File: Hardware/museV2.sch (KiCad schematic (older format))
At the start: 164 parts, among them J1 ATX24, J2 ATX24, P1 RCA_Stero_Jack, P10 AI_RGB, P11 CONN_01X04, P12 AI_RGB, P13 AI_RGB, P14 AI_RGB, P15 AI_RGB, P16 CONN_01X04, P17 AI_RGB, P18 AI_RGB, P19 AI_RGB, P2 CONN_01X06, P20 AI_RGB, P21 AI_RGB, P22 CONN_01X04, P23 AI_RGB, P24 AI_RGB, P25 AI_RGB, P3 3.5mm_Audio, P4 RCA_Stero_Jack, P5 3.5mm_Audio, P6 CONN_01X04, P7 AI_RGB, P8 AI_RGB, P9 AI_RGB, Q1 MOSFET_N, Q10 MOSFET_N, Q11 MOSFET_N, Q12 MOSFET_N, Q13 MOSFET_N, Q2 MOSFET_N, Q3 MOSFET_N, Q4 MOSFET_N, Q5 MOSFET_N, Q6 MOSFET_N, Q7 BSS138, Q8 MOSFET_N, Q9 MOSFET_N, SW1 PWR_BTN, U1 POM-3535L-3-R, U10 PCM1863, U11 PCM1796, U2 PLR135/T10, U3 POM-3535L-3-R, U4 PLT133/T10W, U5 POM-3535L-3-R, U6 POM-3535L-3-R, U7 PCM9211, U8 EdisonConnector, U9 LP38692, X1 24.576 MHz

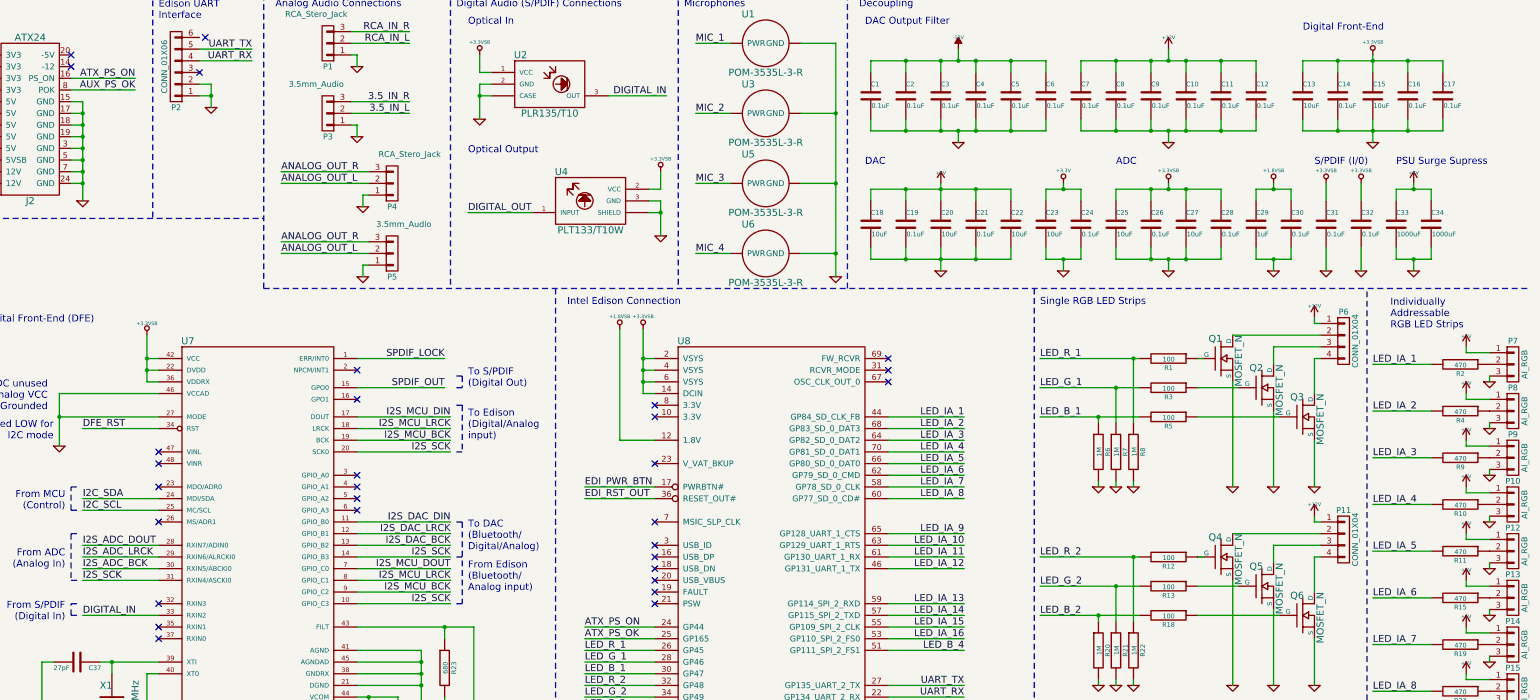
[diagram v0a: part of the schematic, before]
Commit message: Fixed SPDIF labels,
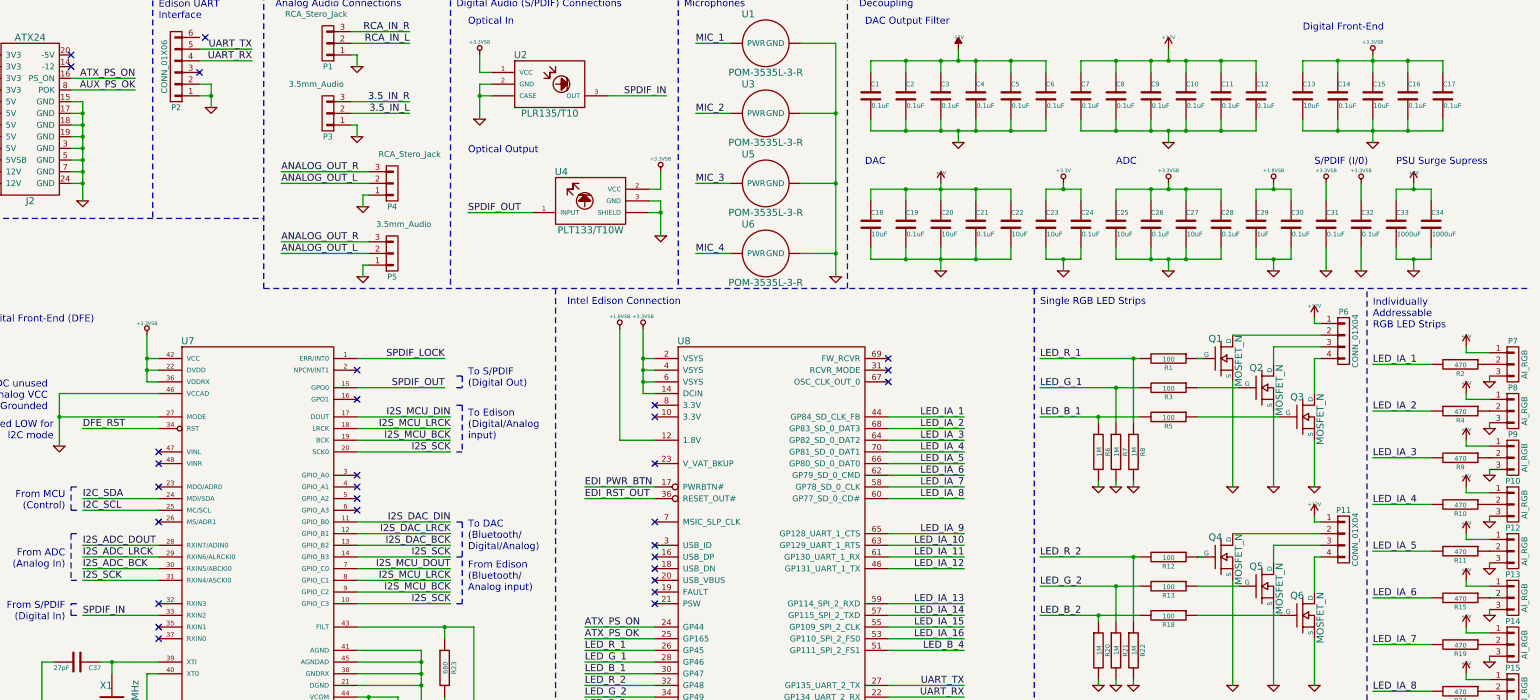
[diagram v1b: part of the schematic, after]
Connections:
- net Audio_Filter/ANALOG_OUT+ is gone; now on net Audio_Filter/ANALOG_OUT+: U11.25 (IOUT_L+)
- net Audio_Filter/ANALOG_OUT- is gone; now on net Audio_Filter/ANALOG_OUT-: U11.26 (IOUT_L-)
- net DIGITAL_OUT is gone; now on net SPDIF_OUT: U4.1 (INPUT)
- net Audio_Filter/ANALOG_OUT+: no longer U11.17 (IOUT_R+)
- net Audio_Filter/ANALOG_OUT-: no longer U11.18 (IOUT_R-)
- net DIGITAL_IN renamed SPDIF_IN
- new net Audio_Filter/ANALOG_OUT+: U11.17 (IOUT_R+)
- new net Audio_Filter/ANALOG_OUT-: U11.18 (IOUT_R-)
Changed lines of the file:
@@
 $EndComp
 Text Label 6950 2400 0    60   ~ 0
-DIGITAL_OUT
+SPDIF_OUT
 Text Label 8650 1400 2    60   ~ 0
-DIGITAL_IN
+SPDIF_IN
 $Comp
 L GND-RESCUE-museV2 #PWR07
@@
 NoConn ~ 4300 6050
 Text Label 3650 5850 0    60   ~ 0
-DIGITAL_IN
+SPDIF_IN
 Text Notes 12500 2000 0    60   ~ 0
 ADC
@@
 Text Notes 11850 3200 0    60   ~ 0
 Single RGB LED Strips
-Text Notes 14850 3400 0    60   ~ 0
+Text Notes 14700 3400 0    60   ~ 0
 Individually \nAddressable\nRGB LED Strips
 $Comp

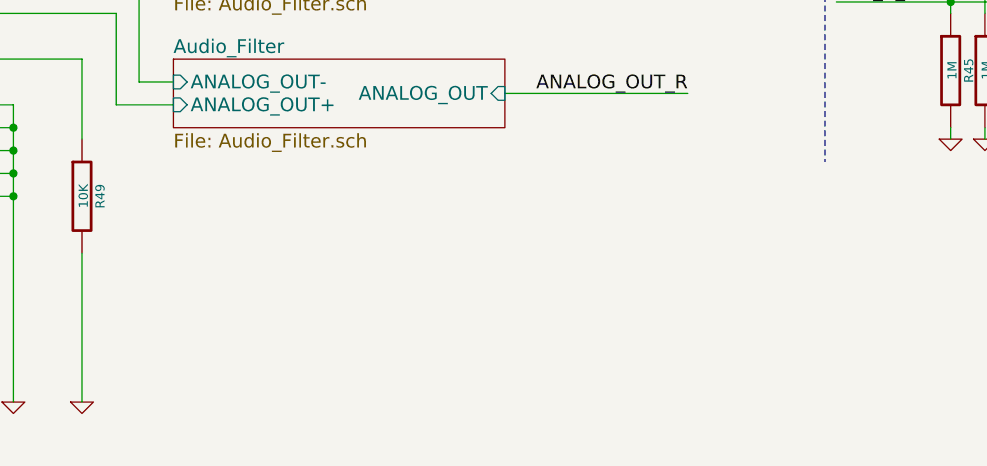
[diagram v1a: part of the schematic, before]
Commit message: Added split rail PS for DAC SB power
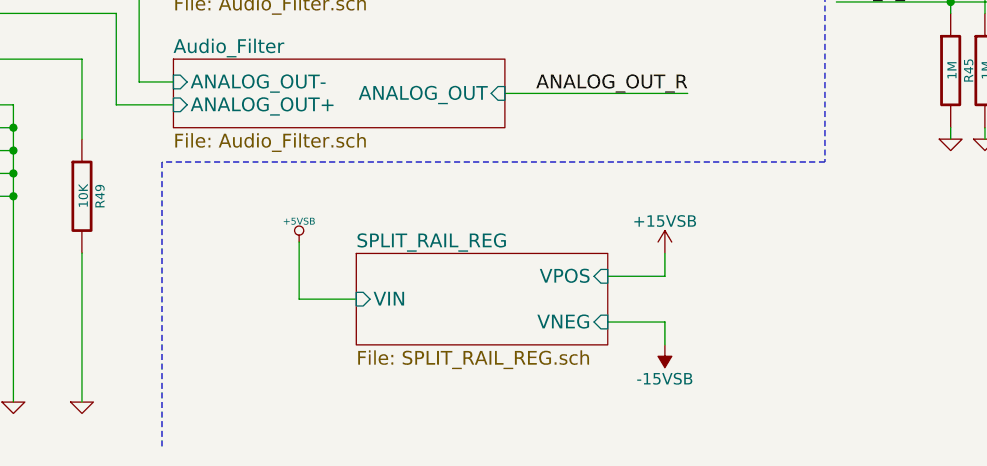
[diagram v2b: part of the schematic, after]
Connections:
- net Audio_Filter/ANALOG_OUT+ is gone; now on net Audio_Filter/ANALOG_OUT+: U11.25 (IOUT_L+)
- net Audio_Filter/ANALOG_OUT- is gone; now on net Audio_Filter/ANALOG_OUT-: U11.26 (IOUT_L-)
- net Audio_Filter/ANALOG_OUT+: no longer U11.17 (IOUT_R+)
- net Audio_Filter/ANALOG_OUT-: no longer U11.18 (IOUT_R-)
- new net Audio_Filter/ANALOG_OUT+: U11.17 (IOUT_R+)
- new net Audio_Filter/ANALOG_OUT-: U11.18 (IOUT_R-)
